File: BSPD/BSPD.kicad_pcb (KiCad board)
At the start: 2 copper layers, 102.9 x 124.7 mm, 55 parts, among them J1 DT13-48PABCD-R015, K1 Latching Relay, Q2 STS6NF20V, Q3 STS6NF20V, U1 LM7805CT, U10 DK1A1B-12V, U11 TLP3122AE, U12 OP AMP, U14 ISO1050DUB, U15 LM7809_TO220, U2 OP AMP, U3 OP AMP, U4 NUCLEO-L432KC, U5 2x4 OR GATE, U6 LM555N, U7 TLP3122AE, U8 NAND, U9 AND GATE

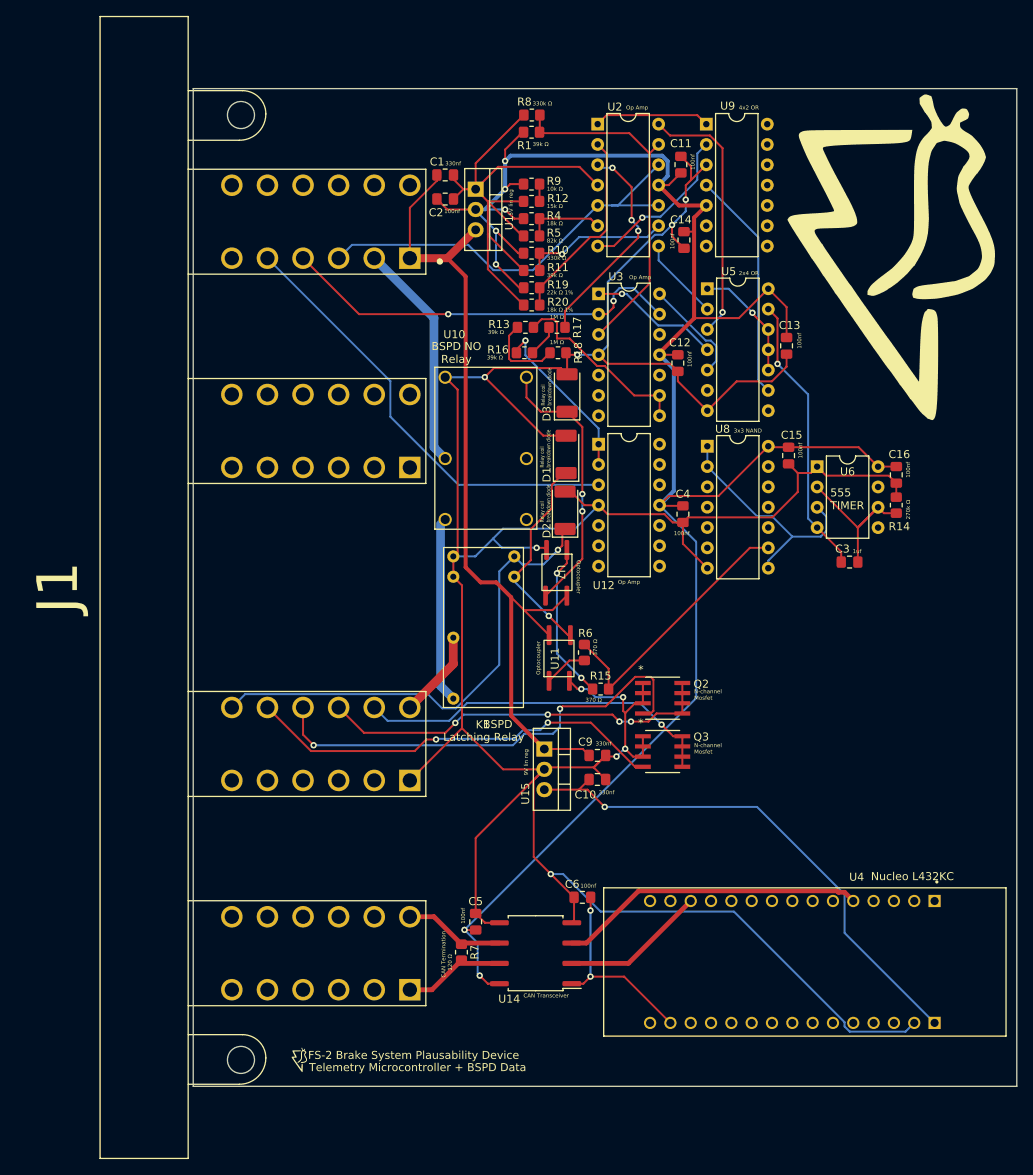
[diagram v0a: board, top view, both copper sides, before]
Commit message: fixed 5v lin reg pins and trace overlapping holes
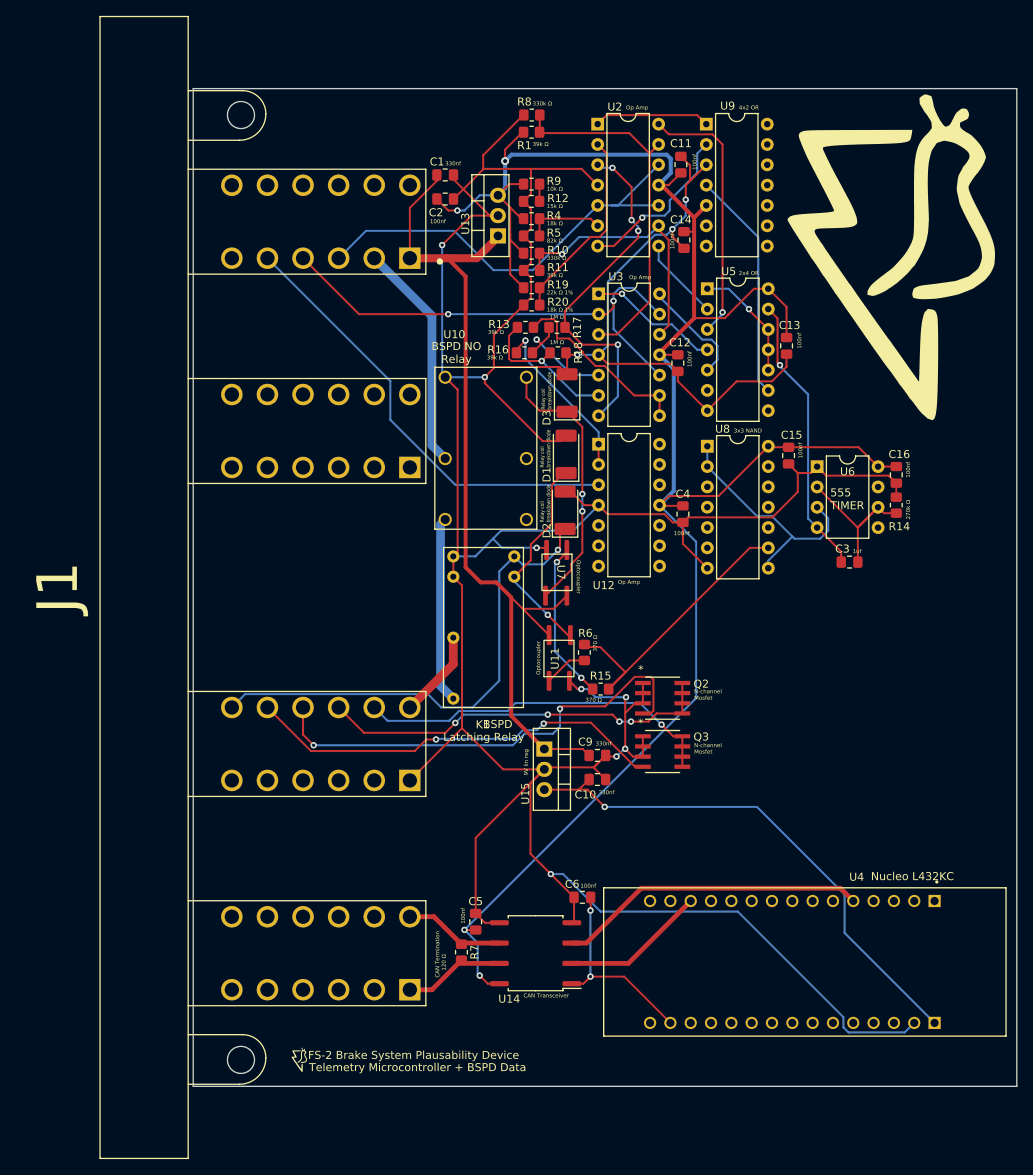
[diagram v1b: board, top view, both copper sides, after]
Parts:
- removed U1: LM7805CT, Package_TO_SOT_THT:TO-220-3_Vertical
- added U13: LM7805_TO220, Package_TO_SOT_THT:TO-220-3_Vertical, F.Cu at (65.2, 41.3)
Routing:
- net GND: track 467.5 -> 492.5 mm, vias 10 -> 11
- net /Current Sensor Differential: track 27.1 -> 44.5 mm, vias 3 -> 4
- net /0.5V: track 18.6 -> 33.2 mm
- net /Current Output: track 51.1 -> 62.8 mm
- net /Current Vref Op: track 4.03 -> 14.4 mm, vias 0 -> 1
- net /Current Output Op: track 10.0 -> 18.9 mm, vias 0 -> 1
- net +5V: track 256.3 -> 252.1 mm, vias 7 -> 4
- net /BSPD Fault Post Timer: track 33.6 -> 36.4 mm
- net +12V: track 107.7 -> 110.3 mm
- net /Brake Output: track 53.3 -> 54.8 mm
- net /4.5V: track 43.9 -> 45.2 mm
- net /SH_RESET: track 61.2 -> 62.2 mm
- net Net-(U6-Q): track 29.9 -> 30.5 mm
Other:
- board text removed: "5V lin reg"

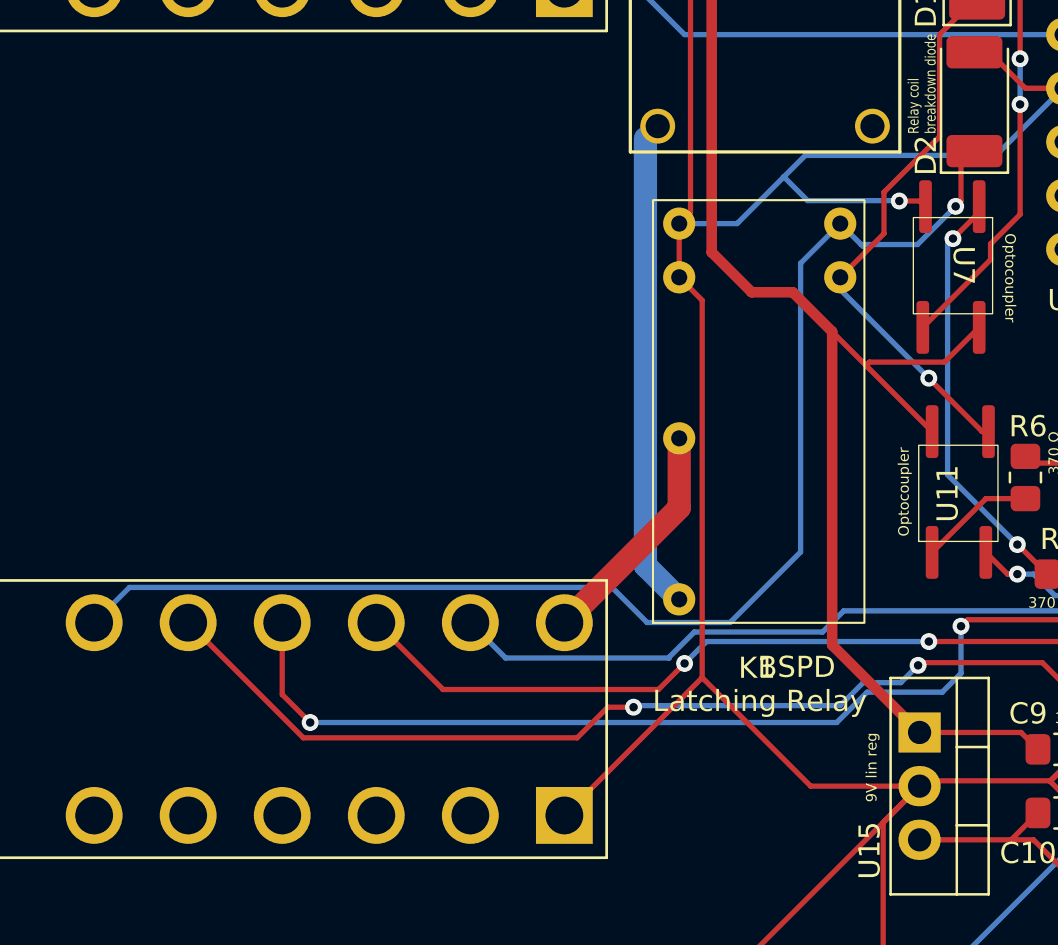
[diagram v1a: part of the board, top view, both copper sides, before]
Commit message: Minor BSPD hole size fix
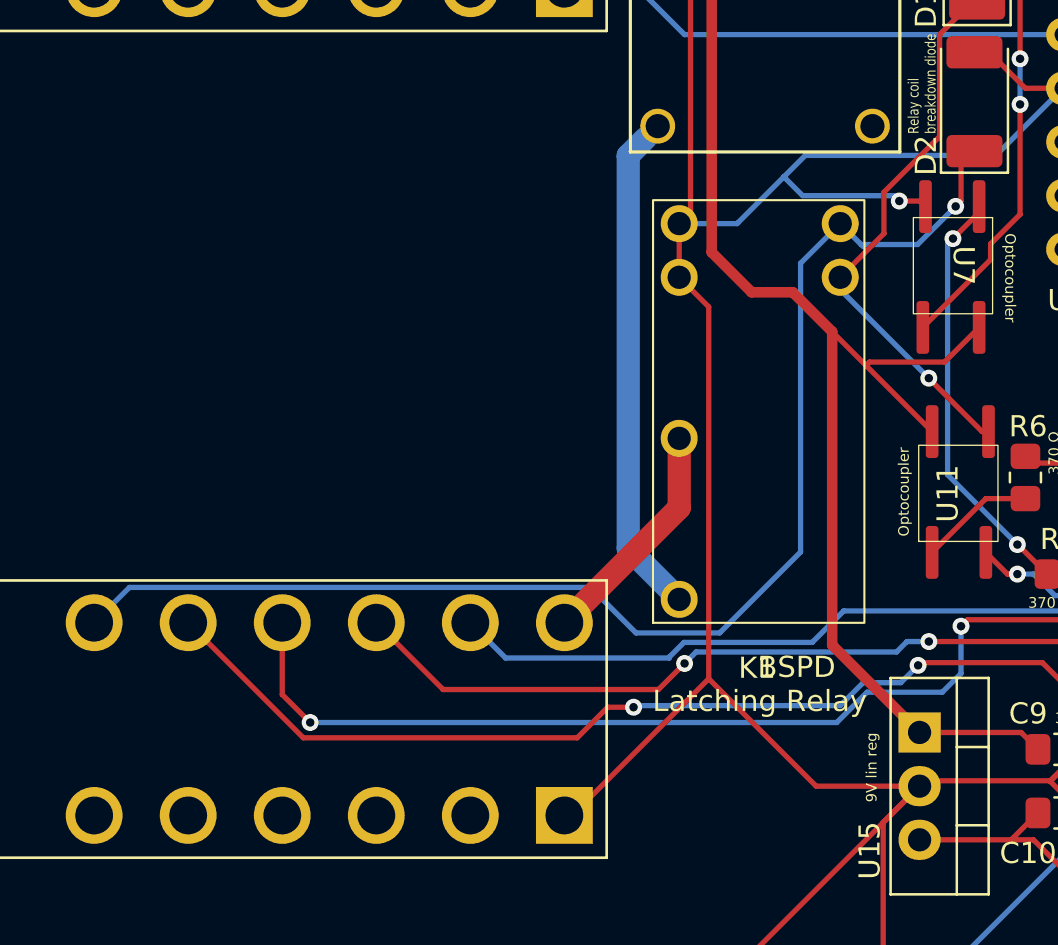
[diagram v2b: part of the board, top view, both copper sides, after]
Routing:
- net Net-(K1-Pad4): track 22.5 -> 23.1 mm

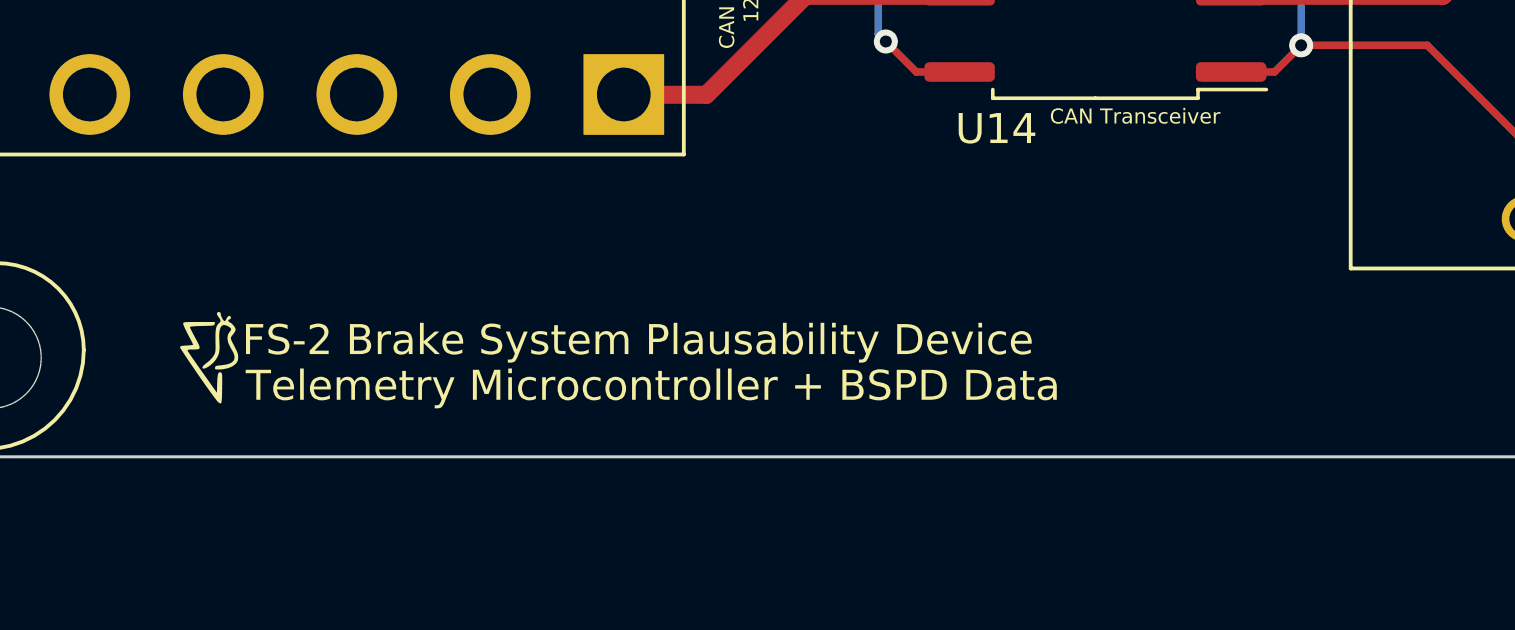
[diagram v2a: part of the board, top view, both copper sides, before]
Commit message: added name to board
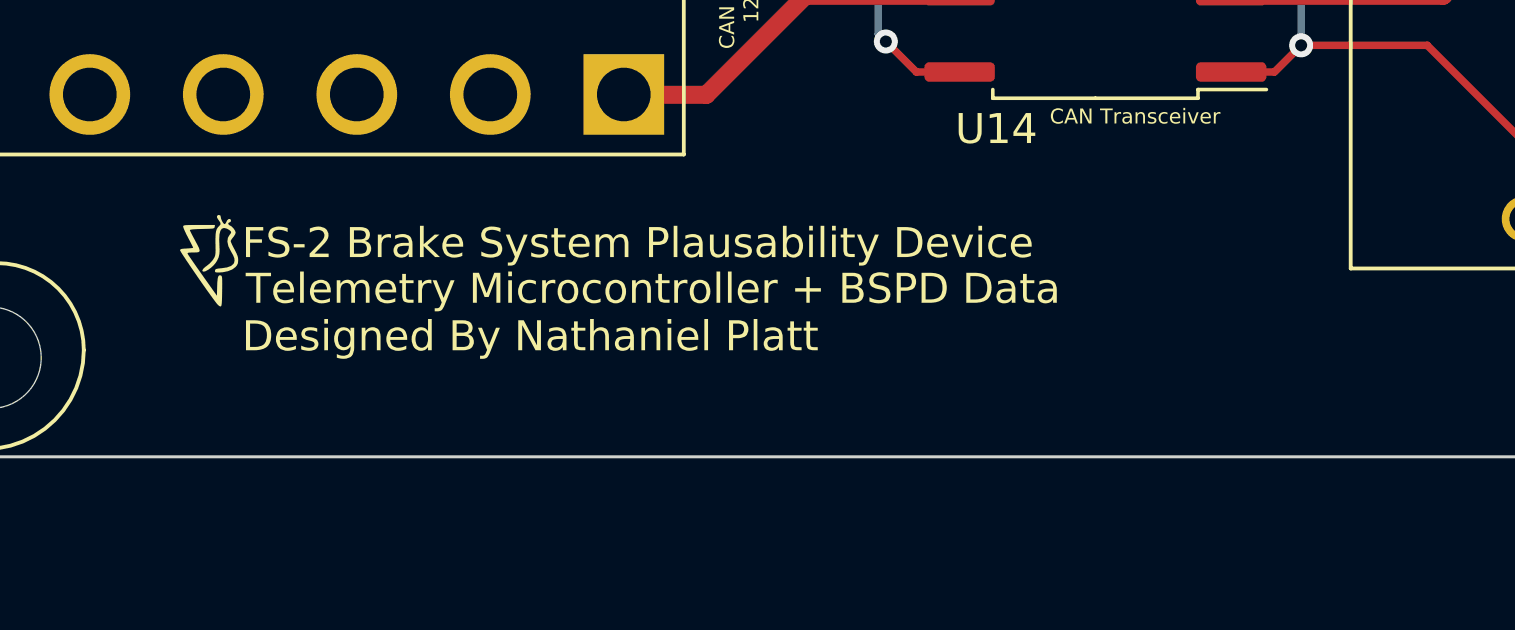
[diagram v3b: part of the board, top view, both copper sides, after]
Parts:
- moved ? 3.23 mm to (43.5, 141.1)
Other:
- board text added: "Designed By Nathaniel Platt"
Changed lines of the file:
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@@
   (net 118 "Net-(R15-Pad1)")
   (footprint "1FS_2_Global_Footprint_Library:FORMULA SLUG" (layer "F.Cu")
-    (at 43.47158 144.330544)
+    (at 43.47158 141.097)
     (property "Sheetfile" "BSPD.kicad_sch")
     (property "Sheetname" "")
@@
     (effects (font (size 0.5 0.5) (thickness 0.075)) (justify left bottom))
   )
-  (gr_text "FS-2 Brake System Plausability Device" (at 41.402 144.272) (layer "F.SilkS")
+  (gr_text "FS-2 Brake System Plausability Device" (at 41.402 141.038456) (layer "F.SilkS")
     (effects (font (size 1 1) (thickness 0.15)) (justify left bottom))
   )
@@
     (effects (font (size 0.5 0.5) (thickness 0.075)) (justify left bottom))
   )
+  (gr_text "Designed By Nathaniel Platt" (at 41.402 144.145) (layer "F.SilkS")
+    (effects (font (size 1 1) (thickness 0.15)) (justify left bottom))
+  )
   (gr_text "39k Ω" (at 63.881 53.594) (layer "F.SilkS")
     (effects (font (size 0.5 0.5) (thickness 0.075)) (justify left bottom))
   )
-  (gr_text "Telemetry Microcontroller + BSPD Data" (at 41.529 145.796) (layer "F.SilkS")
+  (gr_text "Telemetry Microcontroller + BSPD Data" (at 41.529 142.562456) (layer "F.SilkS")
     (effects (font (size 1 1) (thickness 0.15)) (justify left bottom))
   )

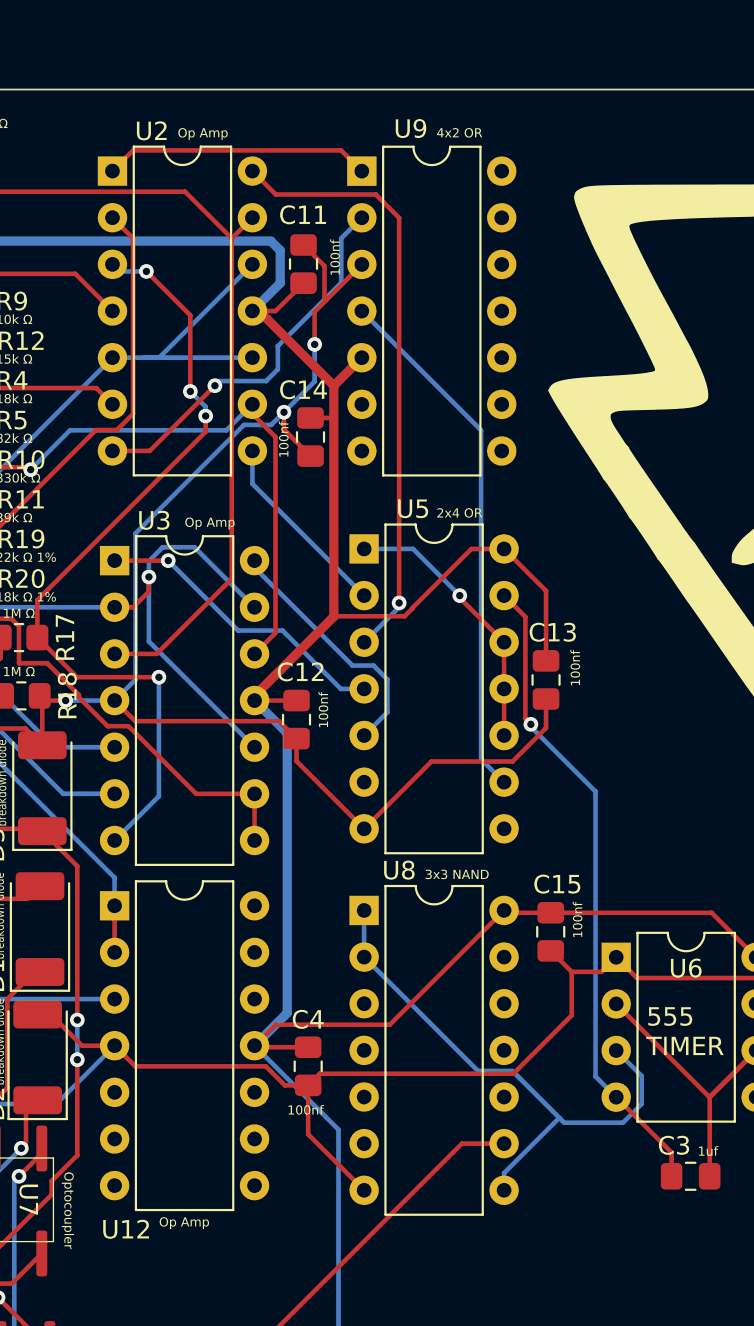
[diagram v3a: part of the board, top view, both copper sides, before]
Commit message: fixed and/nand pins and packages
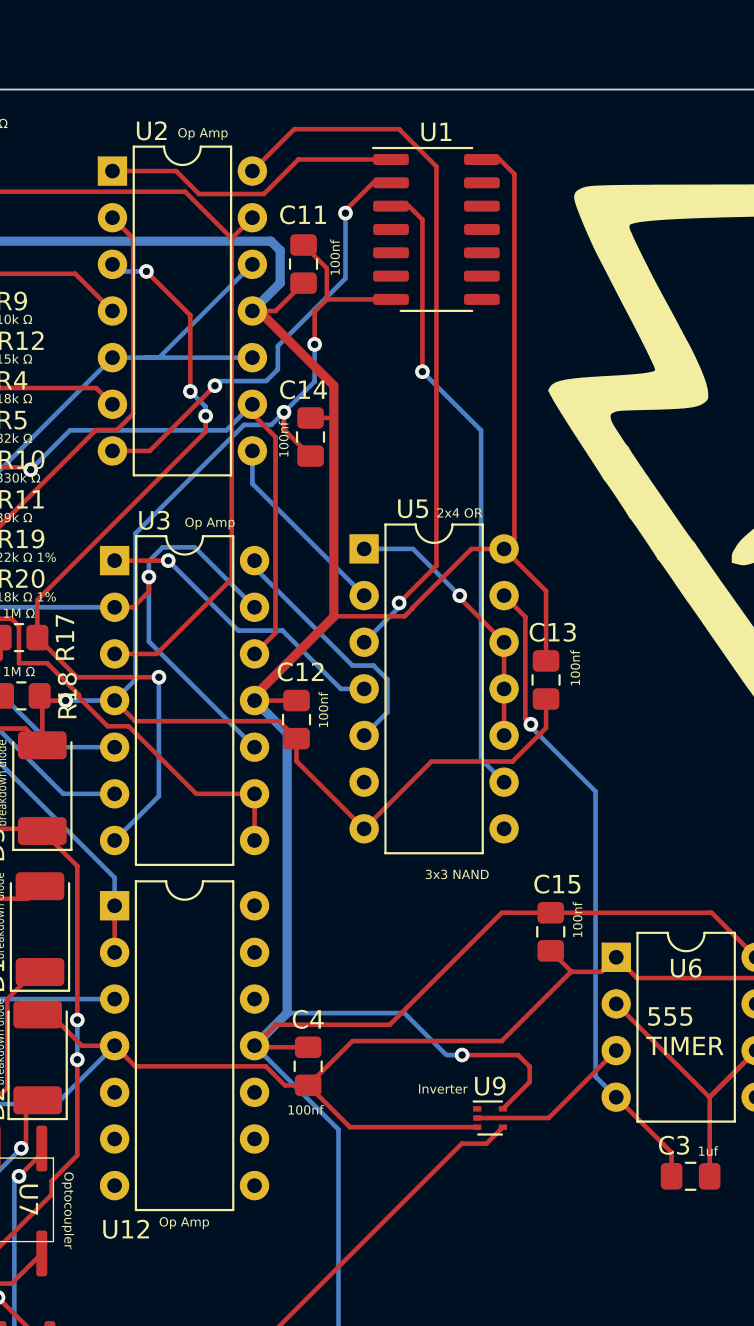
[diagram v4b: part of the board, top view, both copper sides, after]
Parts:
- removed U8: NAND, Package_DIP:DIP-14_W7.62mm
- added U1: 4081, Package_SO:SOIC-14_3.9x8.7mm_P1.27mm, F.Cu at (95.2, 30.5)
- U9: value AND GATE -> 74LVC1GU04DRL; footprint Package_DIP:DIP-14_W7.62mm -> Package_TO_SOT_SMD:SOT-553
- moved U9 52.0 mm to (98.2, 78.9)
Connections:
- U2 pad 1: Net-(U2-Pad1) -> Net-(U1-Pad1)
- U2 pad 7: Net-(U2-Pad7) -> Net-(U1-Pad2)
- U5 pad 9: Net-(U5-Pad9) -> Net-(U1-Pad3)
- U9 pad 1: Net-(U2-Pad1) -> unconnected-(U9-NC-Pad1)
- U9 pad 2: Net-(U2-Pad7) -> Net-(U6-Q)
- U9 pad 4: Net-(U5-Pad9) -> /BSPD Fault Post Timer
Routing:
- net +5V: track 252.1 -> 289.9 mm, vias 4 -> 5
- net Net-(U1-Pad3): track 0.00 -> 34.5 mm, vias 0 -> 1
- net Net-(U5-Pad9): track 28.9 -> 0.00 mm
- net Net-(U1-Pad2): track 0.00 -> 24.1 mm, vias 0 -> 2
- net Net-(U6-Q): track 30.5 -> 9.09 mm
- net Net-(U2-Pad7): track 21.0 -> 0.00 mm, vias 1 -> 0
- net Net-(U1-Pad1): track 0.00 -> 16.5 mm
- net Net-(U2-Pad1): track 14.5 -> 0.00 mm
- net /BrkSenShort: track 32.9 -> 39.3 mm
- net GND: track 492.7 -> 495.2 mm
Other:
- board text added: "Inverter"
- board text removed: "4x2 OR"

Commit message: outputed gerber
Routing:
- net GND: track 495.2 -> 484.7 mm
